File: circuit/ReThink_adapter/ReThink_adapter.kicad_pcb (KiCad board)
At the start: 2 copper layers, 82 x 52 mm, 78 parts, among them J1 FH34SRJ-34S-0.5SH(50), J10 OUT2, J11 OUT3, J2 FH34SRJ-6S-0.5SH(50), J3 Mezzanine, J4 XF3M(1)-3015-1B, J5 XF3M(1)-0815-1B, J6 FH34SRJ-40S-0.5SH(50), J7 FH52-40S-0.5SH, J8 XF3M(1)-1415-1B, J9 OUT1, U1 PCAL6416AHF, U2 LM2775DSG, U3 PCA9306, U4 TPS610333DRLR

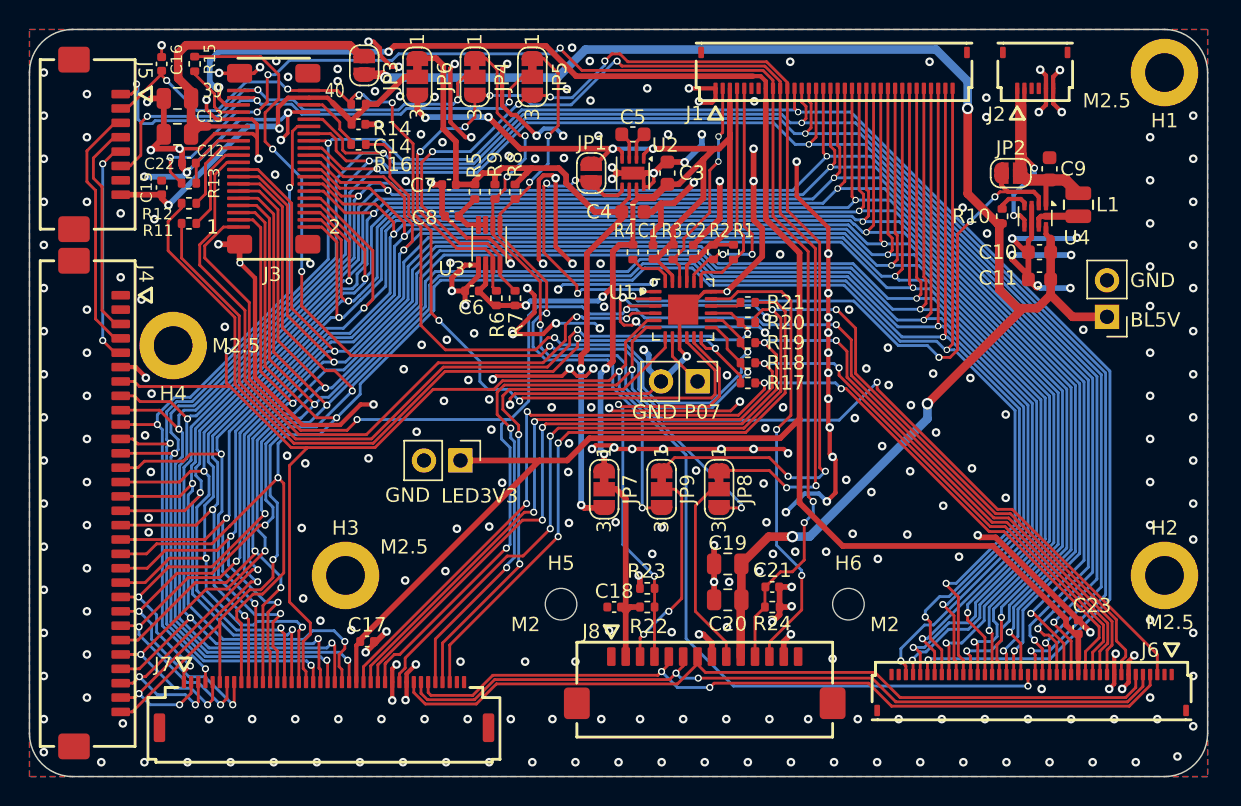
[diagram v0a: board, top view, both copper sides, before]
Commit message: Added connector guide, start adding keyboard mounting holes
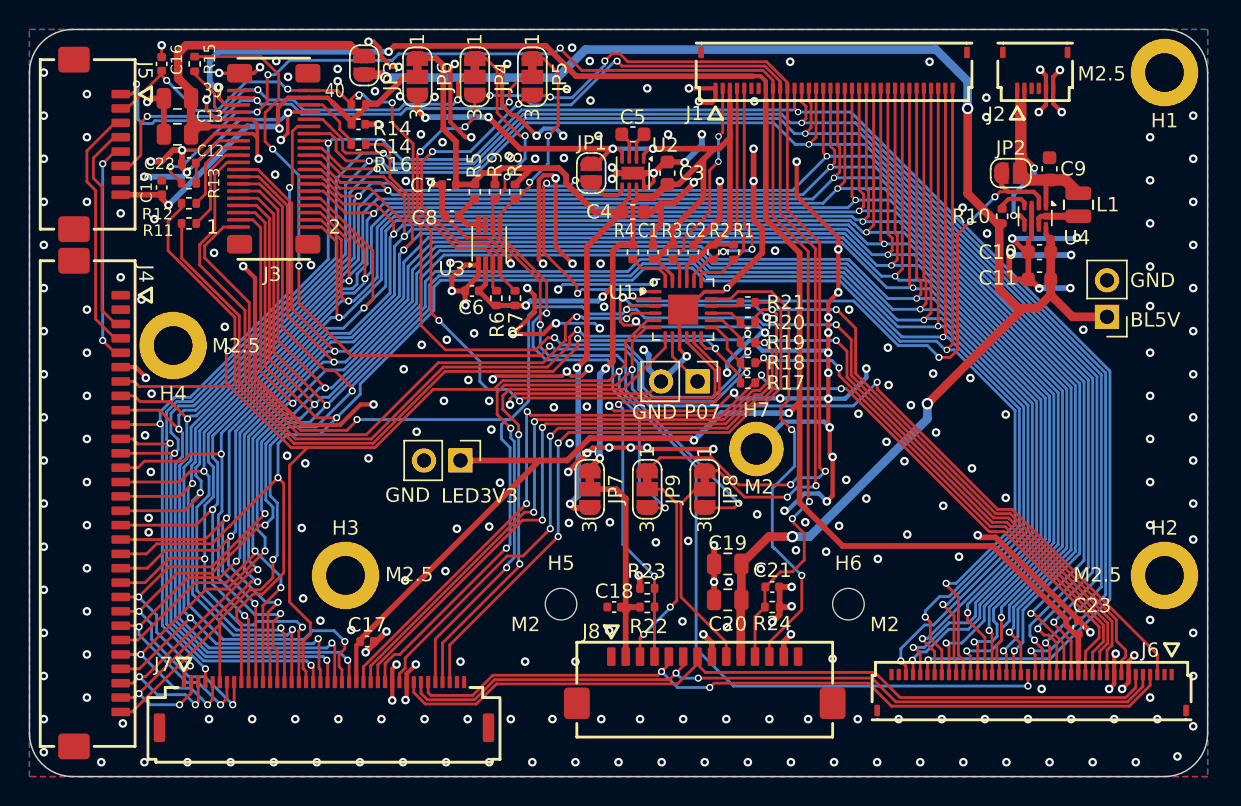
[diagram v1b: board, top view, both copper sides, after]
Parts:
- added H7: M2, MountingHole:MountingHole_2.2mm_M2_ISO14580_Pad, F.Cu at (137.1, 87.2)
- moved JP7 1.00 mm to (125.5, 90.0)
- moved JP8 1.00 mm to (133.5, 90.0)
- moved JP9 1.00 mm to (129.5, 90.0)
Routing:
- net GND: track 341.0 -> 360.3 mm, vias 329 -> 324
- net /FW_CLK: track 79.3 -> 80.9 mm
- net /FW_DAT: track 83.2 -> 84.7 mm
- net TP2_PWR: track 14.3 -> 15.3 mm
- net /DRV16: track 86.4 -> 85.6 mm
- net Net-(J7-Pin_38): track 45.0 -> 44.3 mm
- net Net-(J6-Pin_8): track 86.1 -> 85.5 mm
- net Net-(J6-Pin_11): track 81.9 -> 81.2 mm
- net LED_3V3: track 146.8 -> 147.4 mm, vias 2 -> 4
- net /LS_DAT: track 43.2 -> 43.8 mm
- net /LS_CLK: track 45.8 -> 46.4 mm
- net /KBD_BL_DTCT: track 32.9 -> 33.4 mm
- net /TP2_CLK: track 13.5 -> 14.0 mm
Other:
- board text added: "TODO: - Silkscreen/logos - BOM - Cable guide 3D print - Mounting hole coliding with adapter board, fix!!!"
- board text removed: "TODO: - Silkscreen/logos - BOM - Cable guide 3D print"
